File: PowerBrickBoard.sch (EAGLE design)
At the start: 5 parts

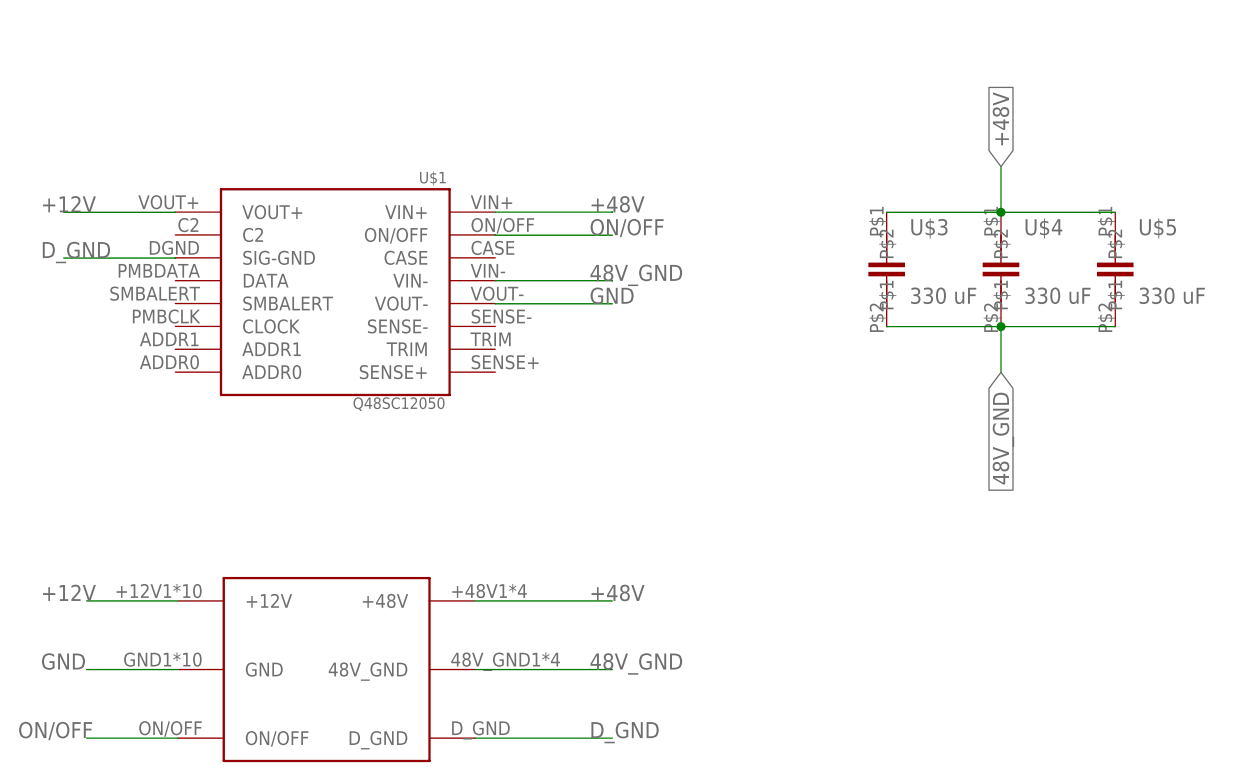
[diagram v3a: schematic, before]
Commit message: respositened capacitors
fixed the board up
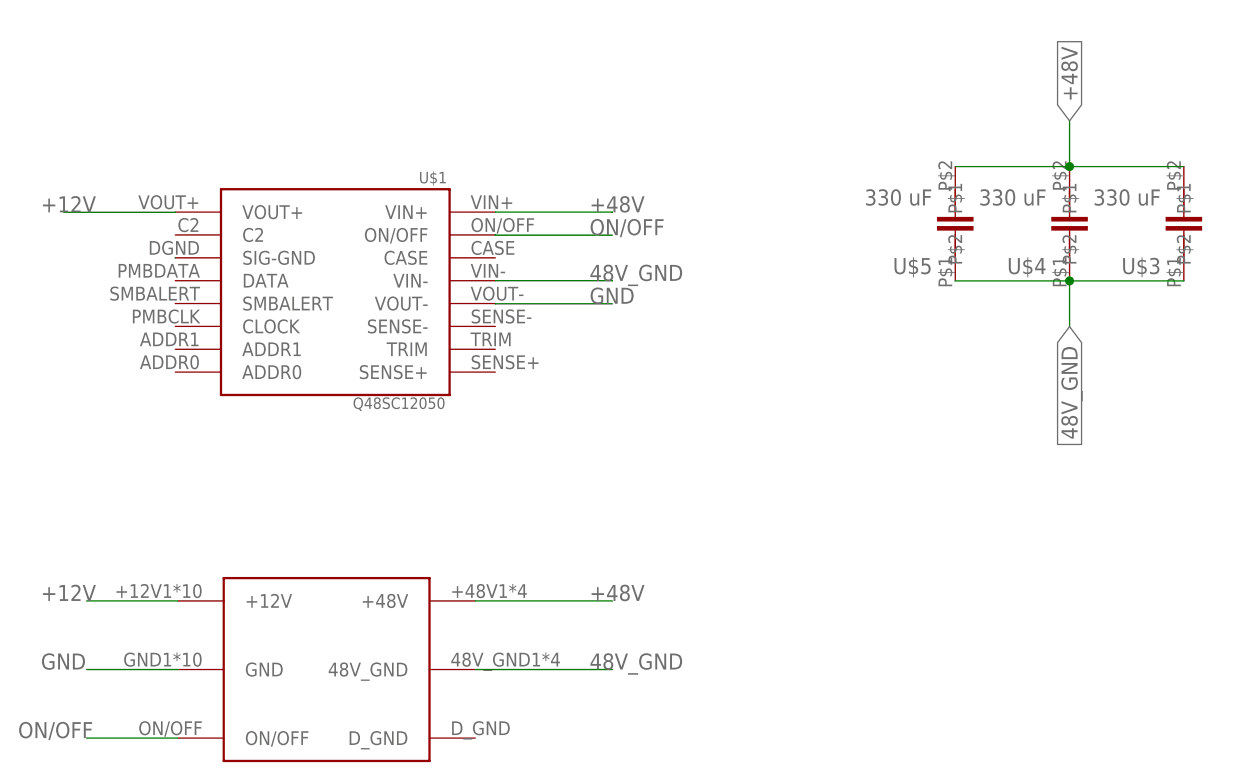
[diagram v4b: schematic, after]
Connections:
- net +48V: now also U$3.P$2, U$4.P$2, U$5.P$2; no longer U$3.P$1, U$4.P$1, U$5.P$1
- net 48V_GND: now also U$3.P$1, U$4.P$1, U$5.P$1; no longer U$3.P$2, U$4.P$2, U$5.P$2
- net D_GND: no longer U$2.D_GND
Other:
- moved on the sheet: U$3, U$4, U$5
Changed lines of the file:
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@@
 <?xml version="1.0" encoding="utf-8"?>
 <!DOCTYPE eagle SYSTEM "eagle.dtd">
-<eagle version="9.2.2">
+<eagle version="9.2.0">
 <drawing>
 <settings>
@@
 </plain>
 <instances>
-<instance part="U$1" gate="G$1" x="55.88" y="137.16" smashed="yes" rot="MR0">
+<instance part="U$1" gate="G$1" x="55.88" y="137.16" rot="MR0">
 <attribute name="NAME" x="67.9958" y="150.5458" size="1.27" layer="95" rot="MR0"/>
 <attribute name="VALUE" x="67.818" y="125.476" size="1.27" layer="95" rot="MR0"/>
 </instance>
-<instance part="FRAME1" gate="G$1" x="0" y="0" smashed="yes">
+<instance part="FRAME1" gate="G$1" x="0" y="0">
 <attribute name="DRAWING_NAME" x="217.17" y="15.24" size="2.54" layer="94"/>
 <attribute name="LAST_DATE_TIME" x="217.17" y="10.16" size="2.286" layer="94"/>
 <attribute name="SHEET" x="230.505" y="5.08" size="2.54" layer="94"/>
 </instance>
-<instance part="U$2" gate="G$1" x="43.18" y="86.36" smashed="yes"/>
-<instance part="U$3" gate="G$1" x="116.84" y="142.24" smashed="yes">
-<attribute name="NAME" x="119.38" y="144.78" size="1.778" layer="95"/>
-<attribute name="VALUE" x="119.38" y="137.16" size="1.778" layer="96"/>
-</instance>
-<instance part="U$4" gate="G$1" x="129.54" y="142.24" smashed="yes">
-<attribute name="NAME" x="132.08" y="144.78" size="1.778" layer="95"/>
-<attribute name="VALUE" x="132.08" y="137.16" size="1.778" layer="96"/>
-</instance>
-<instance part="U$5" gate="G$1" x="142.24" y="142.24" smashed="yes">
-<attribute name="NAME" x="144.78" y="144.78" size="1.778" layer="95"/>
-<attribute name="VALUE" x="144.78" y="137.16" size="1.778" layer="96"/>
+<instance part="U$2" gate="G$1" x="43.18" y="86.36"/>
+<instance part="U$3" gate="G$1" x="149.86" y="144.78" rot="R180">
+<attribute name="NAME" x="147.32" y="142.24" size="1.778" layer="95" rot="R180"/>
+<attribute name="VALUE" x="147.32" y="149.86" size="1.778" layer="96" rot="R180"/>
+</instance>
+<instance part="U$4" gate="G$1" x="137.16" y="144.78" rot="R180">
+<attribute name="NAME" x="134.62" y="142.24" size="1.778" layer="95" rot="R180"/>
+<attribute name="VALUE" x="134.62" y="149.86" size="1.778" layer="96" rot="R180"/>
+</instance>
+<instance part="U$5" gate="G$1" x="124.46" y="144.78" rot="R180">
+<attribute name="NAME" x="121.92" y="142.24" size="1.778" layer="95" rot="R180"/>
+<attribute name="VALUE" x="121.92" y="149.86" size="1.778" layer="96" rot="R180"/>
 </instance>
 </instances>
@@
 <pinref part="U$1" gate="G$1" pin="SIG-GND"/>
 <wire x1="37.7952" y1="142.2654" x2="37.7952" y2="142.24" width="0.1524" layer="91"/>
-<wire x1="37.7952" y1="142.24" x2="25.4" y2="142.24" width="0.1524" layer="91"/>
-<label x="22.86" y="142.24" size="1.778" layer="95"/>
-</segment>
-<segment>
-<pinref part="U$2" gate="G$1" pin="D_GND"/>
-<wire x1="71.12" y1="88.9" x2="86.36" y2="88.9" width="0.1524" layer="91"/>
-<label x="83.82" y="88.9" size="1.778" layer="95"/>
 </segment>
 </net>
@@
 </segment>
 <segment>
-<pinref part="U$3" gate="G$1" pin="P$1"/>
-<pinref part="U$4" gate="G$1" pin="P$1"/>
-<wire x1="116.84" y1="147.32" x2="129.54" y2="147.32" width="0.1524" layer="91"/>
-<pinref part="U$5" gate="G$1" pin="P$1"/>
-<wire x1="129.54" y1="147.32" x2="142.24" y2="147.32" width="0.1524" layer="91"/>
-<junction x="129.54" y="147.32"/>
-<wire x1="129.54" y1="147.32" x2="129.54" y2="152.4" width="0.1524" layer="91"/>
-<label x="129.54" y="152.4" size="1.778" layer="95" rot="R90" xref="yes"/>
+<pinref part="U$3" gate="G$1" pin="P$2"/>
+<pinref part="U$4" gate="G$1" pin="P$2"/>
+<wire x1="149.86" y1="152.4" x2="137.16" y2="152.4" width="0.1524" layer="91"/>
+<pinref part="U$5" gate="G$1" pin="P$2"/>
+<wire x1="137.16" y1="152.4" x2="124.46" y2="152.4" width="0.1524" layer="91"/>
+<junction x="137.16" y="152.4"/>
+<wire x1="137.16" y1="152.4" x2="137.16" y2="157.48" width="0.1524" layer="91"/>
+<label x="137.16" y="157.48" size="1.778" layer="95" rot="R90" xref="yes"/>
 </segment>
 </net>
@@
 </segment>
 <segment>
-<pinref part="U$3" gate="G$1" pin="P$2"/>
-<pinref part="U$4" gate="G$1" pin="P$2"/>
-<wire x1="116.84" y1="134.62" x2="129.54" y2="134.62" width="0.1524" layer="91"/>
-<pinref part="U$5" gate="G$1" pin="P$2"/>
-<wire x1="129.54" y1="134.62" x2="142.24" y2="134.62" width="0.1524" layer="91"/>
-<junction x="129.54" y="134.62"/>
-<wire x1="129.54" y1="134.62" x2="129.54" y2="129.54" width="0.1524" layer="91"/>
-<label x="129.54" y="129.54" size="1.778" layer="95" rot="R270" xref="yes"/>
-</segment>
-</net>
+<pinref part="U$3" gate="G$1" pin="P$1"/>
+<pinref part="U$4" gate="G$1" pin="P$1"/>
+<wire x1="149.86" y1="139.7" x2="137.16" y2="139.7" width="0.1524" layer="91"/>
+<pinref part="U$5" gate="G$1" pin="P$1"/>
+<wire x1="137.16" y1="139.7" x2="124.46" y2="139.7" width="0.1524" layer="91"/>
+<junction x="137.16" y="139.7"/>
+<wire x1="137.16" y1="139.7" x2="137.16" y2="134.62" width="0.1524" layer="91"/>
+<label x="137.16" y="134.62" size="1.778" layer="95" rot="R270" xref="yes"/>
+</segment>
+</net>

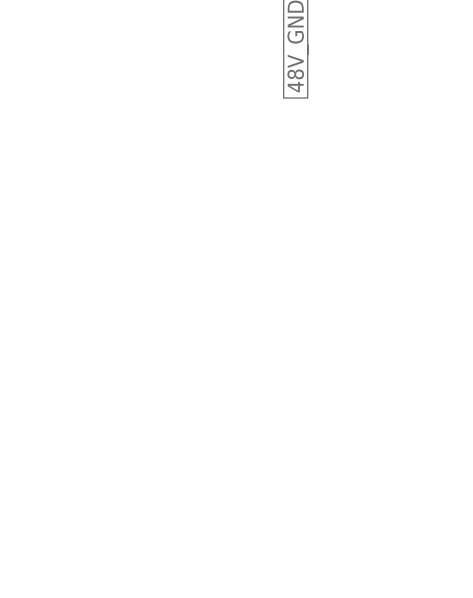
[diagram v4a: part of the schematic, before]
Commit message: added LED
added LED between 12V and GND
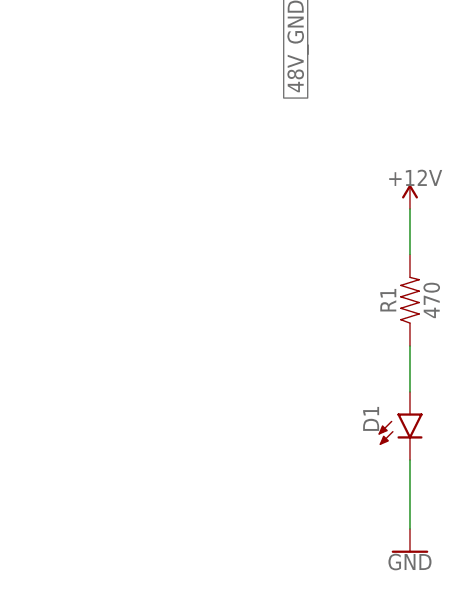
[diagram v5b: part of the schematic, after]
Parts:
- added D1: (no value), SparkFun-LED:LED0603
- added R1: 470, SparkFun-Resistors:RESISTOR0603
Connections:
- new net N$1: D1.A, R1.1
- net +12V: now also R1.2
- net GND: now also D1.C
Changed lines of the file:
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@@
 <layer number="112" name="tSilk" color="7" fill="1" visible="yes" active="yes"/>
 <layer number="113" name="IDFDebug" color="7" fill="1" visible="yes" active="yes"/>
+<layer number="114" name="Badge_Outline" color="7" fill="1" visible="yes" active="yes"/>
+<layer number="115" name="ReferenceISLANDS" color="7" fill="1" visible="yes" active="yes"/>
 <layer number="116" name="Patch_BOT" color="9" fill="4" visible="yes" active="yes"/>
 <layer number="118" name="Rect_Pads" color="7" fill="1" visible="yes" active="yes"/>
@@
 <layer number="230" name="230bmp" color="7" fill="1" visible="yes" active="yes"/>
 <layer number="231" name="231bmp" color="7" fill="1" visible="yes" active="yes"/>
+<layer number="232" name="Eagle3D_PG2" color="7" fill="1" visible="yes" active="yes"/>
+<layer number="233" name="Eagle3D_PG3" color="7" fill="1" visible="yes" active="yes"/>
 <layer number="248" name="Housing" color="7" fill="1" visible="yes" active="yes"/>
 <layer number="249" name="Edge" color="7" fill="1" visible="yes" active="yes"/>
@@
 <part name="U$4" library="UCM1H331MNL1GS" deviceset="UCM1H331MNL1GS" device="" value="330 uF"/>
 <part name="U$5" library="UCM1H331MNL1GS" deviceset="UCM1H331MNL1GS" device="" value="330 uF"/>
+<part name="D1" library="SparkFun-LED" library_urn="urn:adsk.eagle:library:529" deviceset="LED" device="0603" package3d_urn="urn:adsk.eagle:package:39354/1"/>
+<part name="R1" library="SparkFun-Resistors" library_urn="urn:adsk.eagle:library:532" deviceset="RESISTOR" device="0603" package3d_urn="urn:adsk.eagle:package:39650/1" value=" 470"/>
+<part name="GND1" library="SparkFun-PowerSymbols" library_urn="urn:adsk.eagle:library:530" deviceset="GND" device=""/>
+<part name="+12V" library="SparkFun-PowerSymbols" library_urn="urn:adsk.eagle:library:530" deviceset="VCC" device="" value=""/>
 </parts>
 <sheets>
@@
 <attribute name="VALUE" x="121.92" y="149.86" size="1.778" layer="96" rot="R180"/>
 </instance>
+<instance part="D1" gate="G$1" x="149.86" y="86.36">
+<attribute name="NAME" x="146.431" y="84.328" size="1.778" layer="95" font="vector" rot="R90"/>
+<attribute name="VALUE" x="151.765" y="81.788" size="1.778" layer="96" font="vector" rot="R90" align="top-left"/>
+</instance>
+<instance part="R1" gate="G$1" x="149.86" y="99.06" rot="R90">
+<attribute name="NAME" x="148.336" y="99.06" size="1.778" layer="95" font="vector" rot="R90" align="bottom-center"/>
+<attribute name="VALUE" x="151.384" y="99.06" size="1.778" layer="96" font="vector" rot="R90" align="top-center"/>
+</instance>
+<instance part="GND1" gate="1" x="149.86" y="71.12">
+<attribute name="VALUE" x="149.86" y="70.866" size="1.778" layer="96" align="top-center"/>
+</instance>
+<instance part="+12V" gate="G$1" x="149.86" y="109.22">
+<attribute name="VALUE" x="149.86" y="112.014" size="1.778" layer="96" align="bottom-center"/>
+</instance>
 </instances>
 <busses>
@@
 <wire x1="38.1" y1="104.14" x2="27.94" y2="104.14" width="0.1524" layer="91"/>
 <label x="22.86" y="104.14" size="1.778" layer="95"/>
+</segment>
+<segment>
+<pinref part="R1" gate="G$1" pin="2"/>
+<pinref part="+12V" gate="G$1" pin="VCC"/>
+<wire x1="149.86" y1="104.14" x2="149.86" y2="109.22" width="0.1524" layer="91"/>
+<label x="147.32" y="111.76" size="1.778" layer="95"/>
 </segment>
 </net>
@@
 <label x="83.82" y="137.16" size="1.778" layer="95"/>
 </segment>
+<segment>
+<pinref part="D1" gate="G$1" pin="C"/>
+<wire x1="149.86" y1="81.28" x2="149.86" y2="73.66" width="0.1524" layer="91"/>
+<pinref part="GND1" gate="1" pin="GND"/>
+</segment>
 </net>
 <net name="48V_GND" class="0">
@@
 <wire x1="137.16" y1="139.7" x2="137.16" y2="134.62" width="0.1524" layer="91"/>
 <label x="137.16" y="134.62" size="1.778" layer="95" rot="R270" xref="yes"/>
+</segment>
+</net>
+<net name="N$1" class="0">
+<segment>
+<pinref part="D1" gate="G$1" pin="A"/>
+<wire x1="149.86" y1="88.9" x2="149.86" y2="93.98" width="0.1524" layer="91"/>
+<pinref part="R1" gate="G$1" pin="1"/>
 </segment>
 </net>
@@
 will not be understood (or retained) with this version.
 </note>
+<note version="8.3" severity="warning">
+Since Version 8.3, EAGLE supports the association of 3D packages
+with devices in libraries, schematics, and board files. Those 3D
+packages will not be understood (or retained) with this version.
+</note>
 </compatibility>

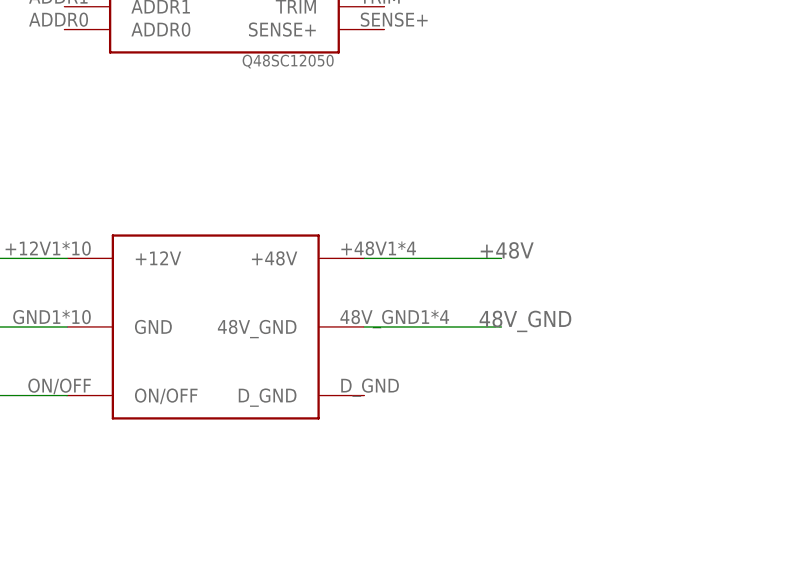
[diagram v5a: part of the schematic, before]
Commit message: added silkscreen
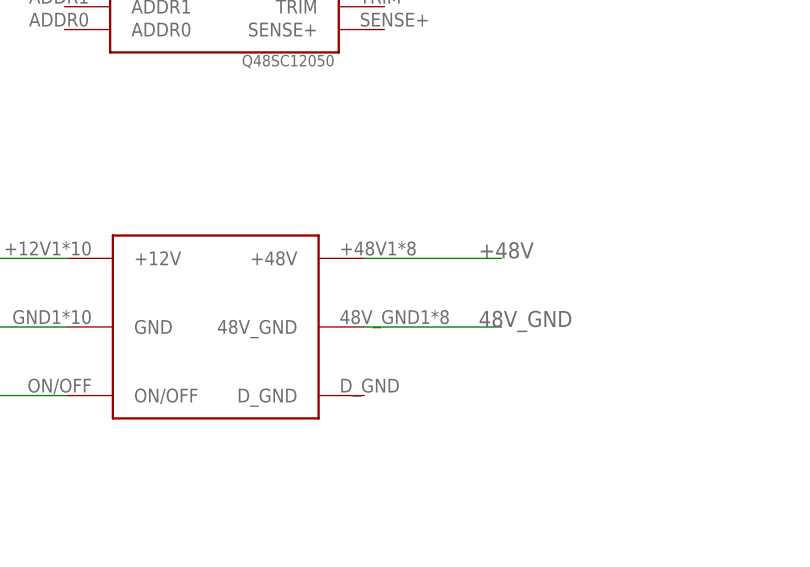
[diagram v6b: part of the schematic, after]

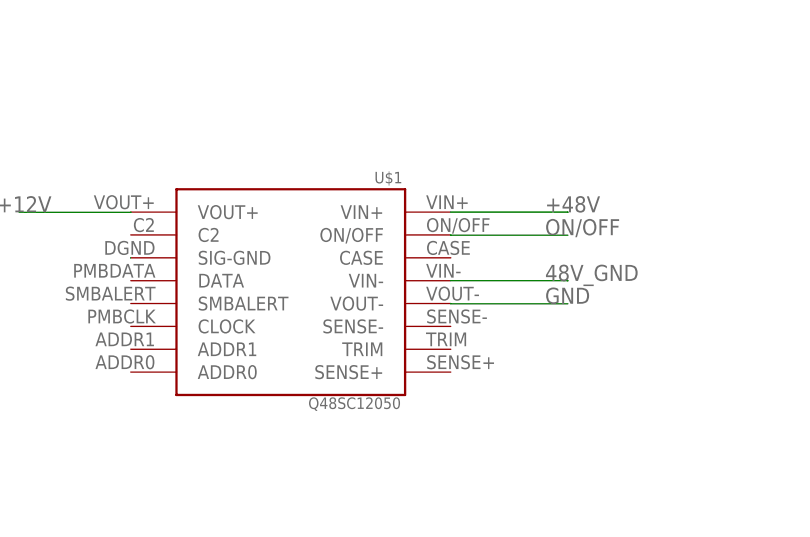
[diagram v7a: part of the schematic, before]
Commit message: updated to jasons desires
changed width sizes and corrected pin layout of on/off switch, added more vias for the overlapping polygon, moved resistor and LED to optimize the +12V polygon
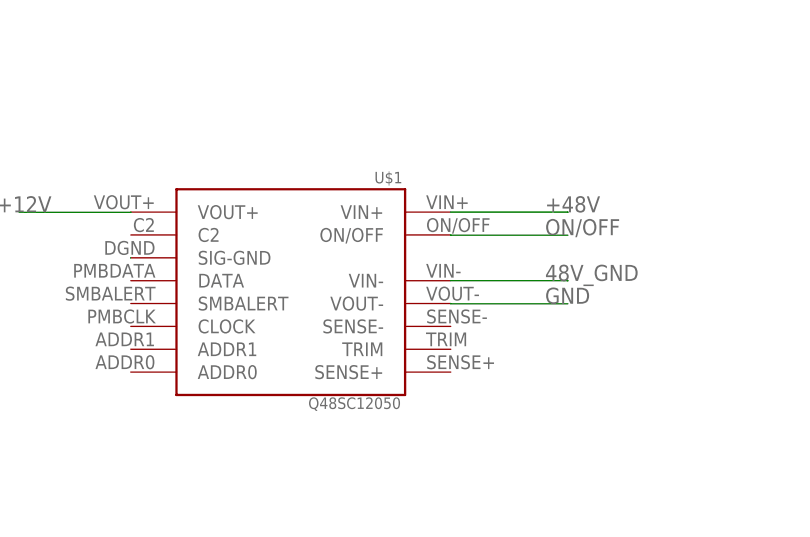
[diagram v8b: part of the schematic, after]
